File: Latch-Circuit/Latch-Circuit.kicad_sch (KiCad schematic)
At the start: 0 parts

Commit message: add title, revision, and date
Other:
- title: (none) -> Latch-Circuit
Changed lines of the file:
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@@
 	(generator_version "9.0")
 	(paper "A4")
+	(title_block
+		(title "Latch-Circuit")
+		(date "2025-11-08")
+		(rev "2.0")
+	)
 	(sheet_instances
 		(path "/"

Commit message: add signal labels and power circuit
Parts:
- added C1: C, ProjectEV_Capacitor:C_3216M, symbol ProjectEV_Capacitor:C_3216M
- added D1: PZ1AH11B-AU_R1_000A1, ProjectEV_Diode:PZ1AH11B-AU_R1_000A1, symbol ProjectEV_Diode:PZ1AH11B-AU_R1_000A1
- added D2: B1911PG--20D000514U1930, ProjectEV_LED:B1911PG--20D000514U1930, symbol ProjectEV_LED:B1911PG--20D000514U1930
- added D3: CUHZ20V,H3F, ProjectEV_Protection:CUHZ20V,H3F, symbol ProjectEV_Protection:CUHZ20V,H3F
- added F1: 0ABB-1000-TM, ProjectEV_Fuse:0ABB-1000-TM, symbol ProjectEV_Fuse:0ABB-1000-TM
- added J1: 2-1445052-2, ProjectEV_Connector:2-1445052-2, symbol ProjectEV_Connector:2-1445052-2
- added J2: 3-794633-8, ProjectEV_Connector:3-794633-8, symbol ProjectEV_Connector:3-794633-8
- added J3: B2P-VH, ProjectEV_Connector_JST:B2P-VH, symbol ProjectEV_Connector_JST:B2P-VH
- added J4: 3-794633-6, ProjectEV_Connector:3-794633-6, symbol ProjectEV_Connector:3-794633-6
- added Q1: DMP3098LQ-7, ProjectEV_Transistor:DMP3098LQ-7, symbol ProjectEV_Transistor:DMP3098LQ-7
- added R1, R2: R, ProjectEV_Resistor:R_1608M, symbol ProjectEV_Resistor:R_1608M
- added R3, R4, R5: 0, ProjectEV_Resistor:R_1608M, symbol ProjectEV_Resistor:R_1608M
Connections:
- new net: D1.2 (A), Q1.1 (G), R1.1
- new net: D3.1 (K), F1.2, Q1.3 (D)
- new net: D2.2 (A), R2.2
- new net +12V: C1.1, D1.1 (K), Q1.2 (S), R2.1
- new net BMS_LED_A: J4.1 (Pin_1)
- new net BMS_LED_K: J4.2 (Pin_2), R3.2
- new net BMS_STATUS: J2.2 (Pin_2)
- new net BSPD_LED_A: J4.3 (Pin_3)
- new net BSPD_LED_K: J4.4 (Pin_4), R4.2
- new net BSPD_STATUS: J2.5 (Pin_5)
- new net GLV_IN: F1.1, J1.1 (Pin_1)
- new net GND: C1.2, D2.1 (K), D3.2 (A), J1.2 (Pin_2), J1.MP1 (MountPin), J1.MP2 (MountPin), J2.1 (Pin_1), J2.4 (Pin_4), J2.MP1 (MountPin), J2.MP2 (MountPin), J4.MP1 (MountPin), J4.MP2 (MountPin), R1.2, R3.1, R4.1, R5.1
- new net IMD_LED_A: J4.5 (Pin_5)
- new net IMD_LED_K: J4.6 (Pin_6), R5.2
- new net IMD_STATUS: J2.3 (Pin_3)
- new net RST_SW1: J2.7 (Pin_7)
- new net RST_SW2: J2.8 (Pin_8)
- no-connect marks 0 -> 1

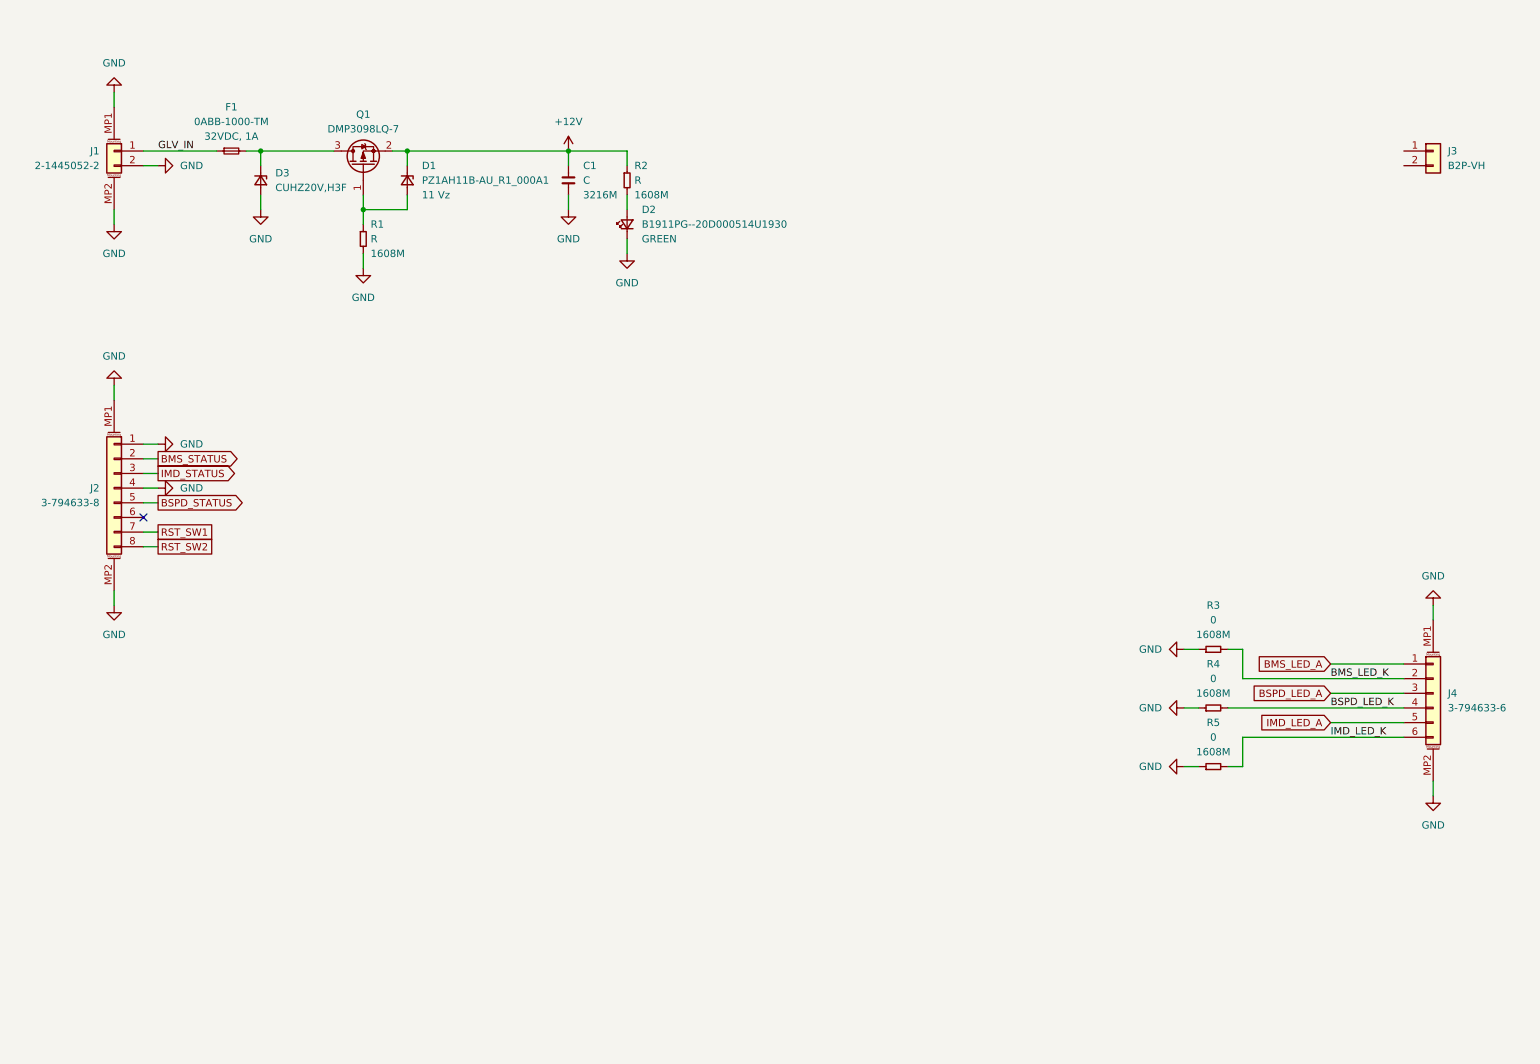
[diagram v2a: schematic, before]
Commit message: complete circuit design, not decide constraints
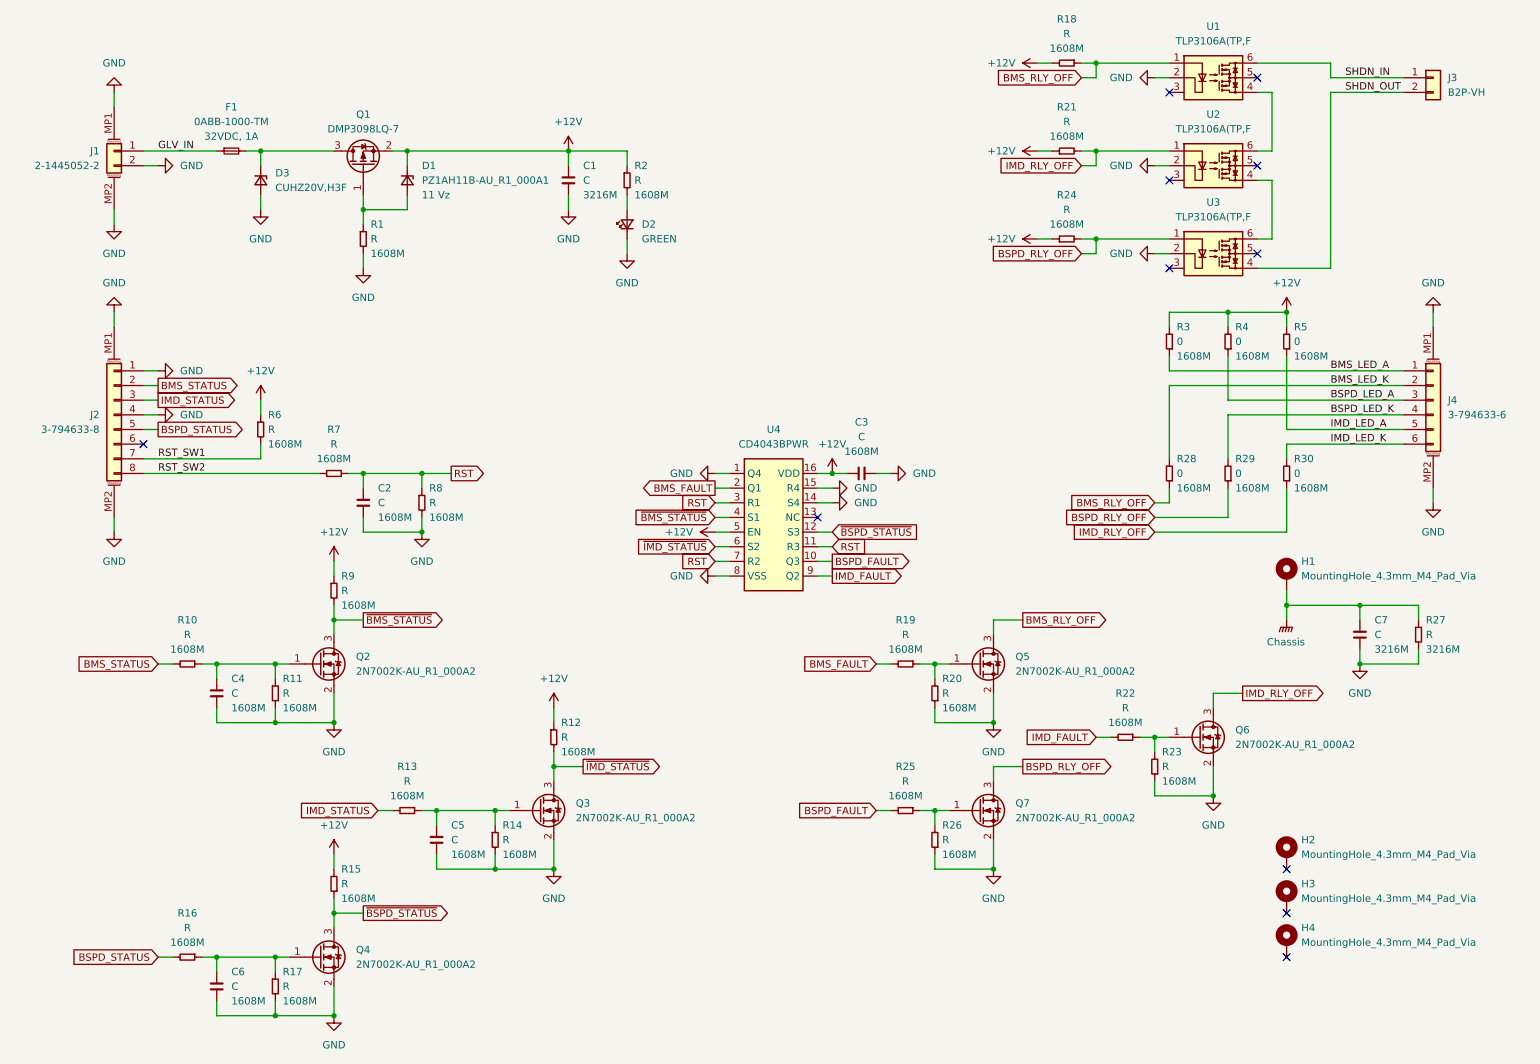
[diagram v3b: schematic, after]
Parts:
- added C2, C3, C4, C5, C6: C, ProjectEV_Capacitor:C_1608M, symbol ProjectEV_Capacitor:C_1608M
- added C7: C, ProjectEV_Capacitor:C_3216M, symbol ProjectEV_Capacitor:C_3216M
- added H1, H2, H3, H4: MountingHole_4.3mm_M4_Pad_Via, ProjectEV_Mechanical:MountingHole_4.3mm_M4_Pad_Via, symbol ProjectEV_Mechanical:MountingHole_4.3mm_M4_Pad_Via
- added Q2, Q3, Q4, Q5, Q6, Q7: 2N7002K-AU_R1_000A2, ProjectEV_Transistor:2N7002K-AU_R1_000A2, symbol ProjectEV_Transistor:2N7002K-AU_R1_000A2
- added R10, R11, R12, R13, R14, R15, R16, R17, R18, R19, R20, R21, R22, R23, R24, R25, R26, R6, R7, R8, R9: R, ProjectEV_Resistor:R_1608M, symbol ProjectEV_Resistor:R_1608M
- added R27: R, ProjectEV_Resistor:R_3216M, symbol ProjectEV_Resistor:R_3216M
- added R28, R29, R30: 0, ProjectEV_Resistor:R_1608M, symbol ProjectEV_Resistor:R_1608M
- added U1, U2, U3: TLP3106A(TP,F, ProjectEV_Relay:TLP3106A(TP,F, symbol ProjectEV_Relay:TLP3106A(TP,F
- added U4: CD4043BPWR, ProjectEV_Logic:CD4043BPWR, symbol ProjectEV_Logic:CD4043BPWR
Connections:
- net +12V: now also R3.2, R4.2, R5.2, C3.1, R12.1, R15.2, R18.2, R21.1, R24.1, R6.1, R9.1, U4.16 (VDD), U4.5 (EN)
- net BMS_LED_A: now also R3.1
- net BMS_LED_K: now also R28.2; no longer R3.2
- net BMS_STATUS: now also R10.2
- net BSPD_LED_A: now also R4.1
- net BSPD_LED_K: now also R29.2; no longer R4.2
- net BSPD_STATUS: now also R16.2
- net GND: now also C2.2, C3.2, C4.2, C5.2, C6.2, C7.2, Q2.2 (S), Q3.2 (S), Q4.2 (S), Q5.2 (S), Q6.2 (S), Q7.2 (S), R11.2, R14.2, R17.2, R20.1, R23.1, R26.1, R27.2, R8.2, U1.2 (Cathode), U2.2 (Cathode), U3.2 (Cathode), U4.1 (Q4), U4.14 (S4), U4.15 (R4), U4.8 (VSS); no longer R3.1, R4.1, R5.1
- net IMD_LED_A: now also R5.1
- net IMD_LED_K: now also R30.2; no longer R5.2
- net IMD_STATUS: now also R13.2
- net RST_SW1: now also R6.2
- net RST_SW2: now also R7.1
- net SHDN_IN: now reaches J3.1 (Pin_1)
- net SHDN_IN: now also U1.6 (Drain)
- net SHDN_OUT: now reaches J3.2 (Pin_2)
- net SHDN_OUT: now also U3.4 (Drain)
- new net: Q5.1 (G), R19.1, R20.2
- new net: C4.1, Q2.1 (G), R10.1, R11.1
- new net: Q6.1 (G), R22.1, R23.2
- new net: C5.1, Q3.1 (G), R13.1, R14.1
- new net: C6.1, Q4.1 (G), R16.1, R17.1
- new net: Q7.1 (G), R25.1, R26.2
- new net: U2.4 (Drain), U3.6 (Drain)
- new net: U1.4 (Drain), U2.6 (Drain)
- new net BMS_FAULT: R19.2, U4.2 (Q1)
- new net BMS_RLY_OFF: Q5.3 (D), R18.1, R28.1, U1.1 (Anode)
- new net BSPD_FAULT: R25.2, U4.10 (Q3)
- new net BSPD_RLY_OFF: Q7.3 (D), R24.2, R29.1, U3.1 (Anode)
- new net Chassis: C7.1, H1.MP, R27.1
- new net IMD_FAULT: R22.2, U4.9 (Q2)
- new net IMD_RLY_OFF: Q6.3 (D), R21.2, R30.1, U2.1 (Anode)
- new net RST: C2.1, R7.2, R8.1, U4.11 (R3), U4.3 (R1), U4.7 (R2)
- new net ~{BMS_STATUS}: Q2.3 (D), R9.2, U4.4 (S1)
- new net ~{BSPD_STATUS}: Q4.3 (D), R15.1, U4.12 (S3)
- new net ~{IMD_STATUS}: Q3.3 (D), R12.2, U4.6 (S2)
- no-connect marks 1 -> 11
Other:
- moved on the sheet: J2, J3, J4, R3, R4, R5

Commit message: modify pin assigns, decide consts, and apply some changes
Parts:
- removed R18, R21, R24: R, ProjectEV_Resistor:R_1608M, symbol ProjectEV_Resistor:R_1608M
- added R18, R21, R24: 1.2k, ProjectEV_Resistor:R_3216M, symbol ProjectEV_Resistor:R_3216M
- C1: value C -> 22u
- C2, C4, C5, C6: value C -> 10n
- C3: value C -> 100n
- C7: value C -> 1n
- R1, R12, R15, R2, R8, R9: value R -> 10k
- R10, R13, R16, R19, R22, R25, R7: value R -> 100
- R11, R14, R17, R20, R23, R26: value R -> 100k
- R27: value R -> 1M
- R6: value R -> 0
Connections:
- net +12V: now also R18.1, R21.1, R24.1
- net BMS_LED_K: now also J4.4 (Pin_4); no longer J4.2 (Pin_2)
- net BMS_RLY_OFF: now also R18.2
- net BMS_STATUS: now also J2.5 (Pin_5); no longer J2.2 (Pin_2)
- net BSPD_LED_A: now also J4.2 (Pin_2); no longer J4.3 (Pin_3)
- net BSPD_LED_K: now also J4.5 (Pin_5); no longer J4.4 (Pin_4)
- net BSPD_RLY_OFF: now also R24.2
- net BSPD_STATUS: now also J2.7 (Pin_7); no longer J2.5 (Pin_5)
- net GND: now also J2.3 (Pin_3); no longer J2.4 (Pin_4)
- net IMD_LED_A: now also J4.3 (Pin_3); no longer J4.5 (Pin_5)
- net IMD_RLY_OFF: now also R21.2
- net IMD_STATUS: now also J2.6 (Pin_6); no longer J2.3 (Pin_3)
- net RST_SW1: now also J2.4 (Pin_4); no longer J2.7 (Pin_7)
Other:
- moved on the sheet: C3, R6, U4

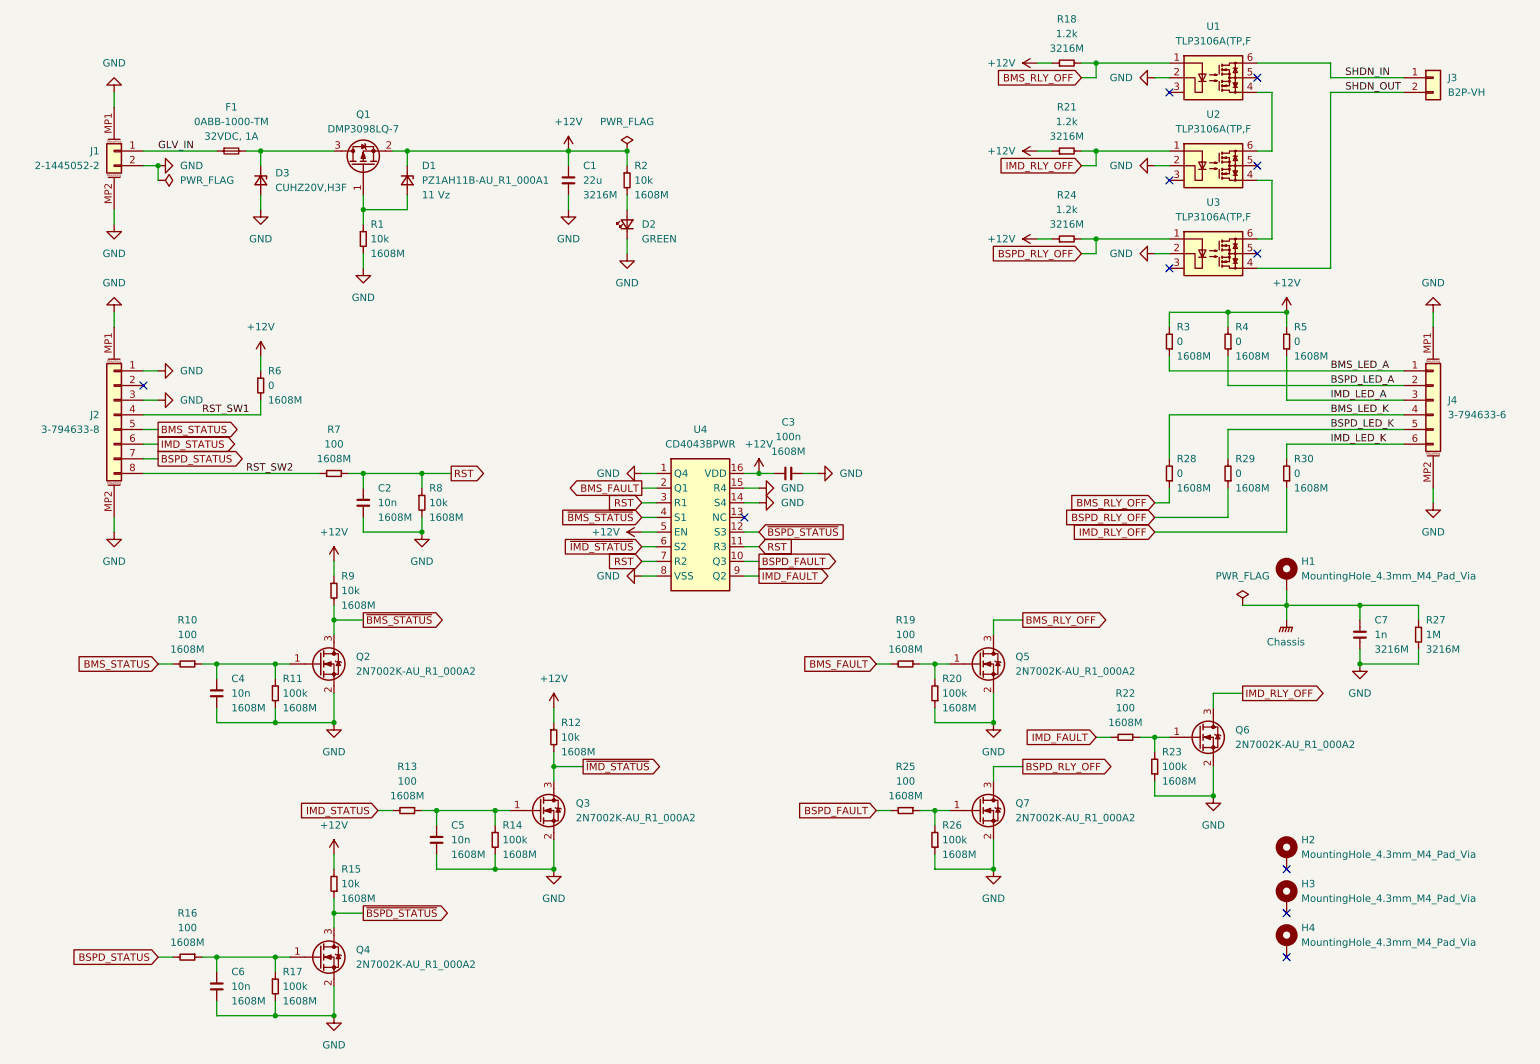
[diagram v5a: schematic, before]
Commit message: add LEDs
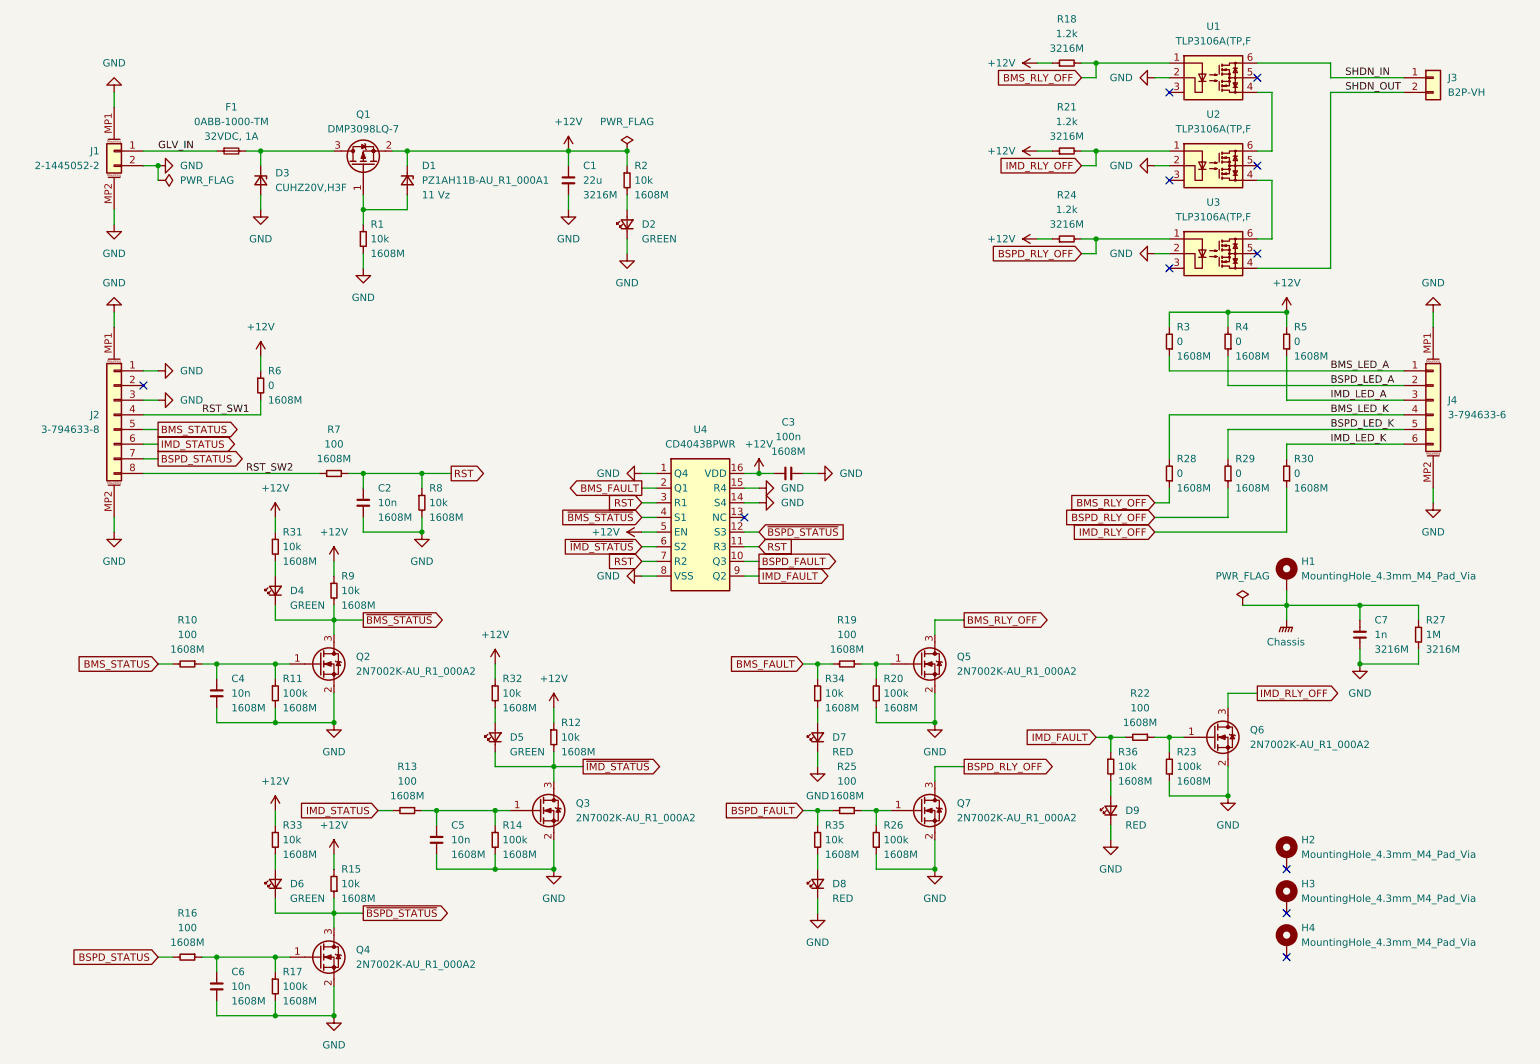
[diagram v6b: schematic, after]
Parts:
- added D4, D5, D6: B1911PG--20D000514U1930, ProjectEV_LED:B1911PG--20D000514U1930, symbol ProjectEV_LED:B1911PG--20D000514U1930
- added D7, D8, D9: B1911USD-20D000114U1930, ProjectEV_LED:B1911USD-20D000114U1930, symbol ProjectEV_LED:B1911USD-20D000114U1930
- added R31, R32, R33, R34, R35, R36: 10k, ProjectEV_Resistor:R_1608M, symbol ProjectEV_Resistor:R_1608M
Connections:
- net +12V: now also R31.1, R32.1, R33.1
- net BMS_FAULT: now also R34.1
- net BSPD_FAULT: now also R35.1
- net GND: now also D7.1 (K), D8.1 (K), D9.1 (K)
- net IMD_FAULT: now also R36.1
- net ~{BMS_STATUS}: now also D4.1 (K)
- net ~{BSPD_STATUS}: now also D6.1 (K)
- net ~{IMD_STATUS}: now also D5.1 (K)
- new net: D9.2 (A), R36.2
- new net: D8.2 (A), R35.2
- new net: D6.2 (A), R33.2
- new net: D4.2 (A), R31.2
- new net: D7.2 (A), R34.2
- new net: D5.2 (A), R32.2
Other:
- moved on the sheet: Q5, Q6, Q7, R19, R20, R22, R23, R25, R26
